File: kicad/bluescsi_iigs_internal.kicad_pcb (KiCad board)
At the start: 2 copper layers, 61.5 x 55.4 mm, 27 parts, among them J1 Conn_02x13_Odd_Even, J2 Conn_02x13_Odd_Even, J3 105162-0001, J4 Conn_01x02_Male, J5 Conn_01x02_Male, J6 DB25_Male, M1 Screw_Terminal_01x01, M2 Screw_Terminal_01x01, SW1 SW_SPDT, U1 YAAJ_BluePill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

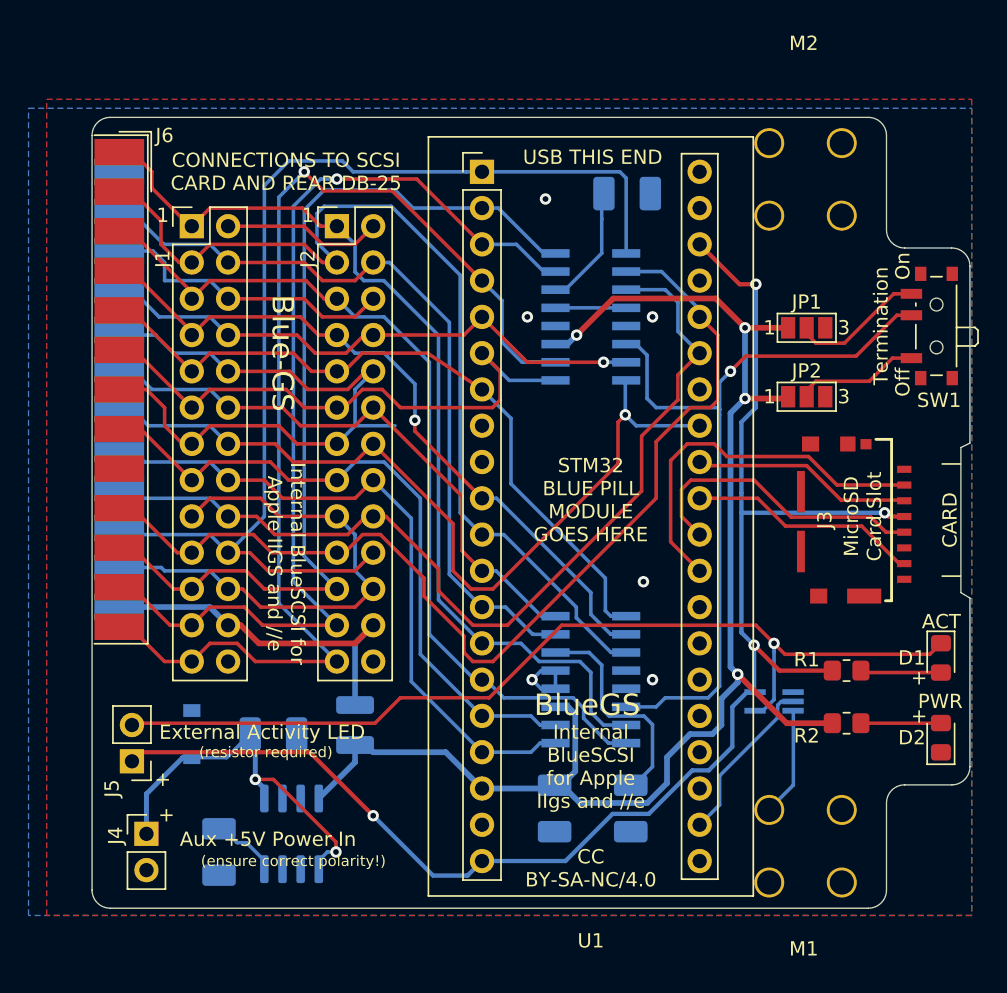
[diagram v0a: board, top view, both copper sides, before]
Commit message: Increase card indent, change C5 footprint
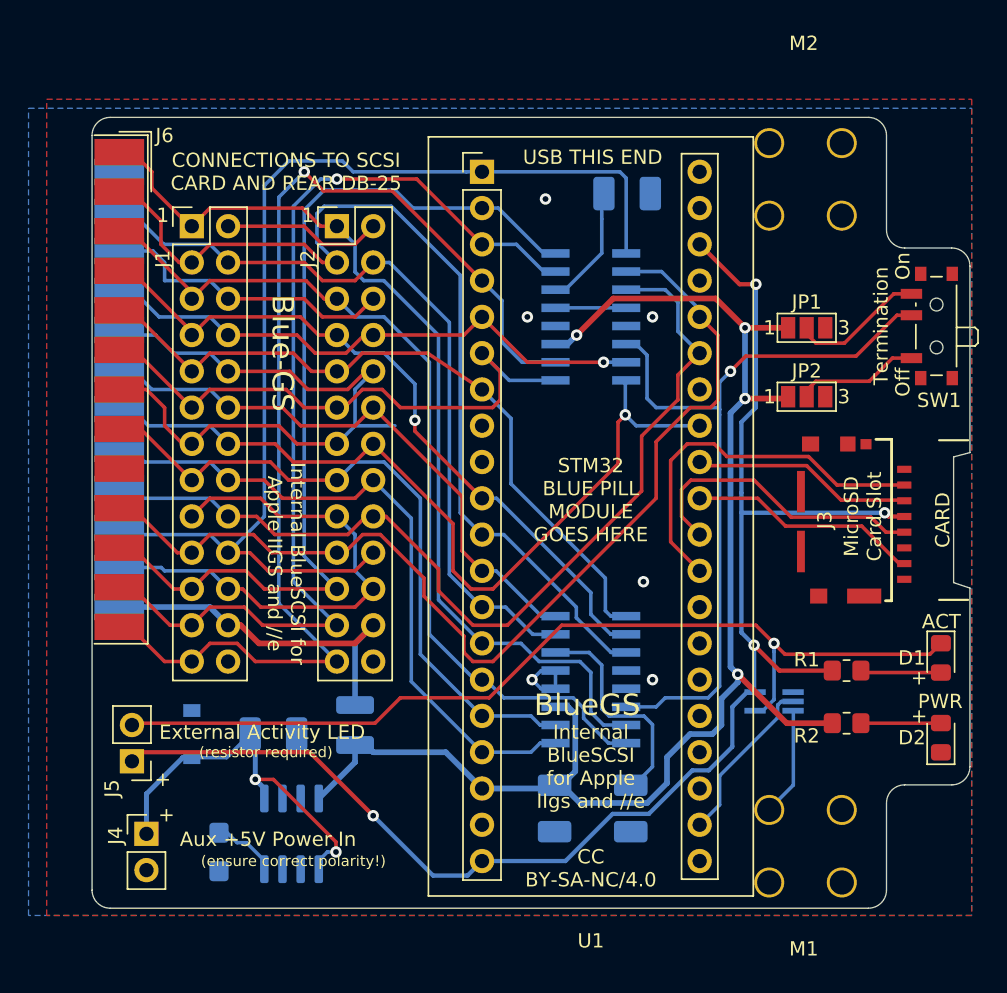
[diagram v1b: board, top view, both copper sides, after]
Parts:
- C1, C2: value 4.7uF, 6.3v -> 2.2uF, 6.3v
- C5: footprint Capacitor_Tantalum_SMD:CP_EIA-3528-21_Kemet-B_Pad1.50x2.35mm_HandSolder -> Capacitor_Tantalum_SMD:CP_EIA-3216-10_Kemet-I
- R1: value 110 -> 100
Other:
- outline, holes or cut-outs redrawn
- board text added: "CARD"
- board text removed: "| CARD |"

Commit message: Added compatibility for 74LVC1G125SE in place of NL17SZ07DFT2G
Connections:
- U5 pad 1: unconnected-(U5-Pad1) -> GND
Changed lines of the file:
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@@
   (net 51 "/SCSI_TERMPWR")
   (net 52 "Net-(D1-Pad2)")
-  (net 53 "unconnected-(U5-Pad1)")
   (footprint "my library:YAAJ_BluePill_2" (layer "F.Cu")
     (at 152.4 50.8)
@@
     (tags "capacitor tantalum")
     (property "DESCRIPTION" "2.2uF 6.3V CASE-B_3528 Tantalum Capacitor")
-    (property "LCSC part number" "C19276")
+    (property "LCSC part number" "C444753")
     (property "MANUFACTURER_NAME" "Kyocera AVX")
-    (property "MANUFACTURER_PART_NUMBER" "TAJB225K035RNJ")
+    (property "MANUFACTURER_PART_NUMBER" "TAJB225M020RNJ")
     (property "Sheetfile" "bluescsi_iigs_internal.kicad_sch")
     (property "Sheetname" "")
@@
     (tags "capacitor tantalum")
     (property "DESCRIPTION" "4.7uF 6.3V CASE-B_3528 Tantalum Capacitor")
-    (property "LCSC part number" "C7204")
-    (property "MANUFACTURER_NAME" "Kyocera AVX")
-    (property "MANUFACTURER_PART_NUMBER" "TAJB475K016RNJ")
+    (property "LCSC part number" "C918865")
+    (property "MANUFACTURER_NAME" "KEMET")
+    (property "MANUFACTURER_PART_NUMBER" "T494B475K016AT")
     (property "Sheetfile" "bluescsi_iigs_internal.kicad_sch")
     (property "Sheetname" "")
@@
     (tags "capacitor tantalum")
     (property "DESCRIPTION" "2.2uF 6.3V CASE-B_3528 Tantalum Capacitor")
-    (property "LCSC part number" "C19276")
+    (property "LCSC part number" "C444753")
     (property "MANUFACTURER_NAME" "Kyocera AVX")
-    (property "MANUFACTURER_PART_NUMBER" "TAJB225K035RNJ")
+    (property "MANUFACTURER_PART_NUMBER" "TAJB225M020RNJ")
     (property "Sheetfile" "bluescsi_iigs_internal.kicad_sch")
     (property "Sheetname" "")
@@
     (fp_line (start -0.675 0.6) (end -0.675 -1.1) (layer "B.Fab") (width 0.1))
     (pad "1" smd rect locked (at -1.33 0.65 180) (size 1.5 0.4) (layers "B.Cu" "B.Paste" "B.Mask")
-      (net 53 "unconnected-(U5-Pad1)") (pinfunction "Pin_1") (pintype "passive+no_connect"))
+      (net 13 "GND") (pinfunction "Pin_1") (pintype "passive"))
     (pad "2" smd rect locked (at -1.33 0 180) (size 1.5 0.4) (layers "B.Cu" "B.Paste" "B.Mask")
       (net 50 "/DISK_ACT") (pinfunction "Pin_2") (pintype "passive"))
@@
     (tags "capacitor tantalum")
     (property "DESCRIPTION" "1uF 6.3V CASE-B_3528 Tantalum Capacitor")
-    (property "LCSC part number" "C7192")
-    (property "MANUFACTURER_NAME" "Kyocera AVX")
-    (property "MANUFACTURER_PART_NUMBER" "TAJB105K035RNJ")
+    (property "LCSC part number" "C452761")
+    (property "MANUFACTURER_NAME" "KEMET")
+    (property "MANUFACTURER_PART_NUMBER" "T491B105K025AT")
     (property "Sheetfile" "bluescsi_iigs_internal.kicad_sch")
     (property "Sheetname" "")
@@
   )
   (gr_text "Internal BlueSCSI for\nApple IIGS and //e\n" (at 138.684 78.232 270) (layer "F.SilkS")
-    (effects (font (size 1 1) (thickness 0.15)))
+    (effects (font (size 1 1) (thickness 0.125)))
   )
   (gr_text "PWR" (at 186.055 87.884) (layer "F.SilkS")

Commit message: Push traces around, remove a hyphen
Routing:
- net +3V3: track 106.0 -> 105.2 mm, vias 4 -> 3
- net /SCSI_RST: track 50.1 -> 49.5 mm
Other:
- board text removed: "Blue-GS"

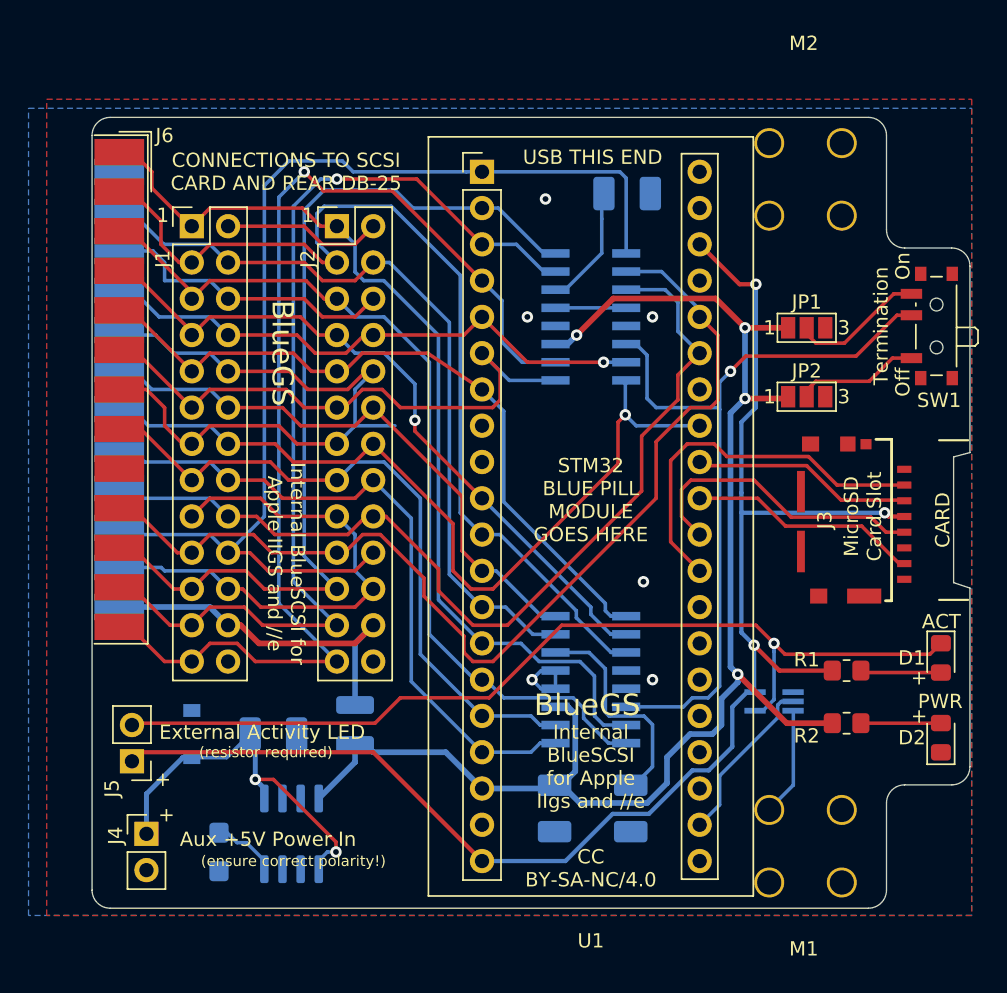
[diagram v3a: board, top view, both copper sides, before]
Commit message: Make name more consistent, move sinkscreens around to make things look better
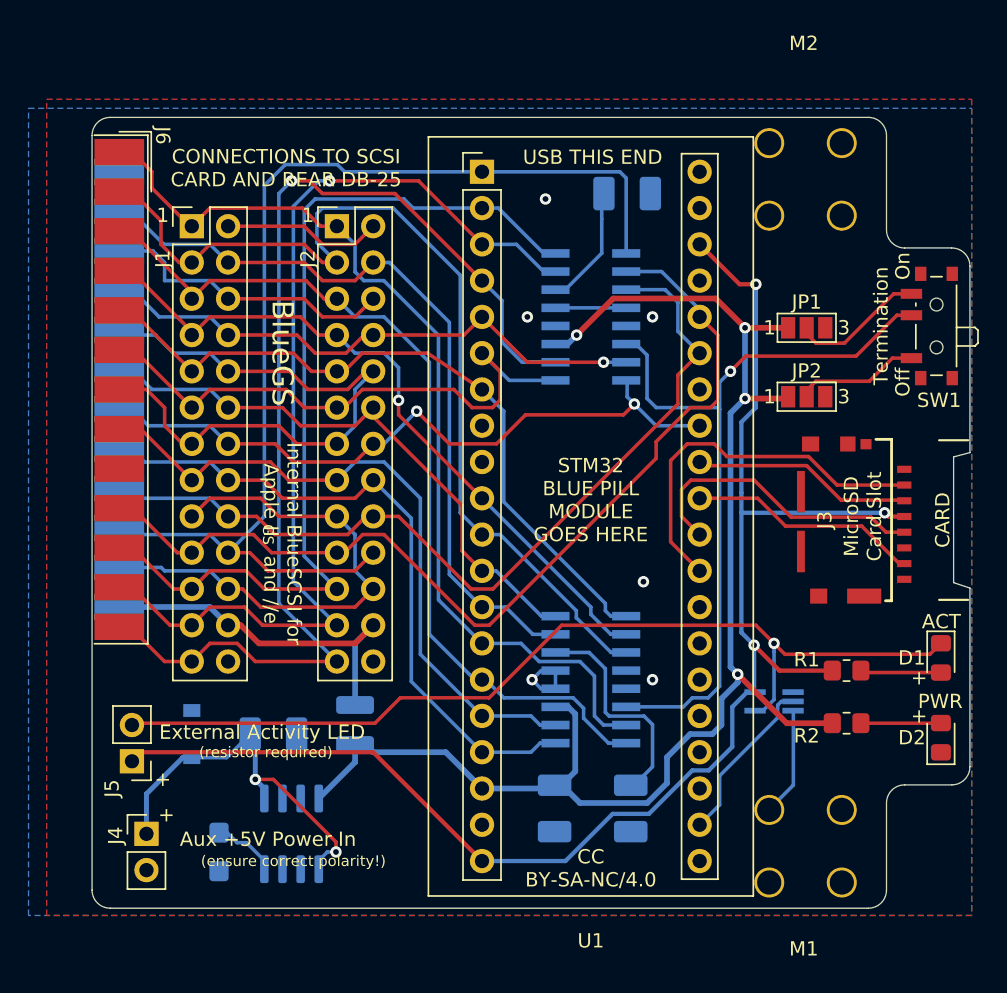
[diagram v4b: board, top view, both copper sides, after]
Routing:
- net /SCSI_DBP: track 58.3 -> 48.1 mm, vias 1 -> 2
- net /SCSI_DB3: track 72.9 -> 67.7 mm
- net /SCSI_DB2: track 65.9 -> 60.8 mm
- net GND: track 134.2 -> 131.4 mm
- net /SCSI_DB5: track 65.0 -> 64.5 mm
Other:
- board text added: "GS"
- board text added: "Internal BlueSCSI for Apple II and //e"
- board text added: "v1.4 (12/2022)"
- board text removed: "Internal BlueSCSI for Apple IIGS and //e"
- board text removed: "Internal BlueSCSI for Apple IIgs and //e"
- board text removed: "v1.4 (11/2022)"

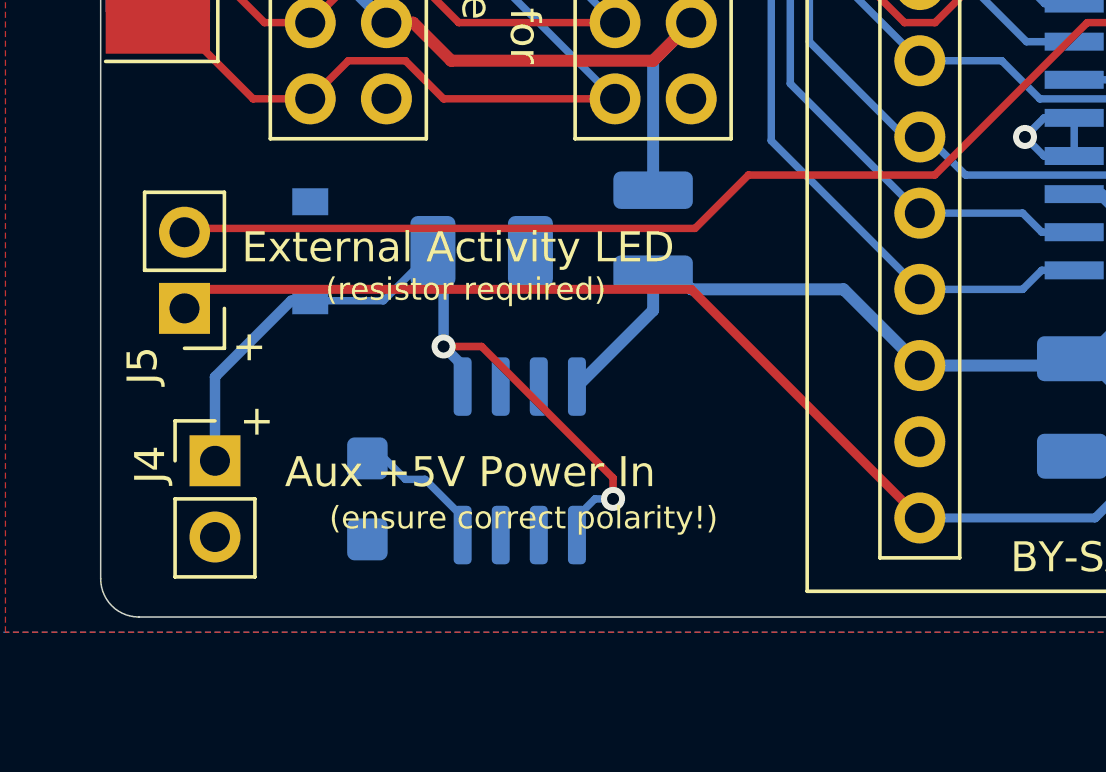
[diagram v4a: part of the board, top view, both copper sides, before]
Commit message: Move power controller to front for better wire clearance in tight cases
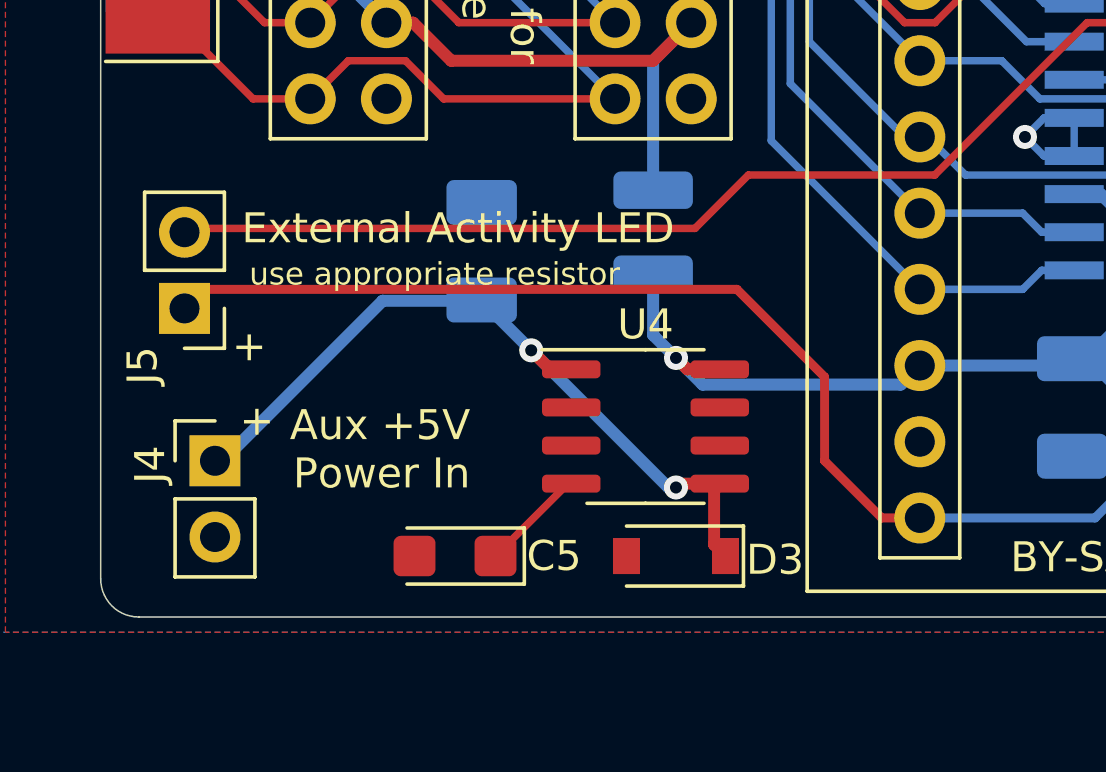
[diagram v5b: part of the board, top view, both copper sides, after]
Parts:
- C5, D3, U4: moved to F.Cu
- moved D3 15.9 mm to (144.3, 100.3), turned to 180 degrees
- moved U4 4.34 mm to (143.3, 96.0), turned to 0 degrees
- moved C5 3.49 mm to (136.9, 100.3), turned to 180 degrees
- turned C4 to 90 degrees
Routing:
- net +3V3: track 105.2 -> 106.8 mm
- net +5V: track 101.7 -> 100.2 mm, vias 4 -> 5
- net Net-(C5-Pad1): track 4.70 -> 3.52 mm
- net /+5V_AUX: track 26.9 -> 25.9 mm
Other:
- board text added: "check the polarity!"
- board text added: "use appropriate resistor"
- board text removed: "(ensure correct polarity!)"
- board text removed: "(resistor required)"

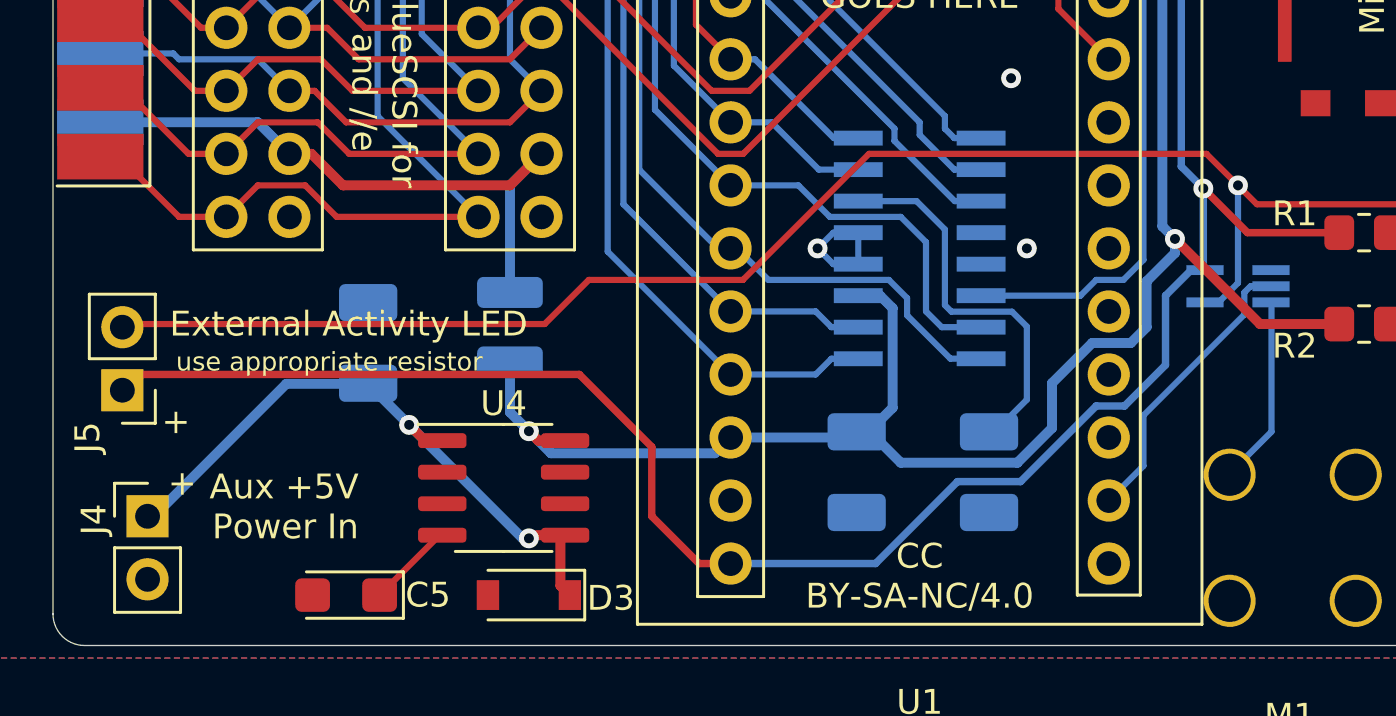
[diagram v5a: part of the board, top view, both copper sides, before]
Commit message: Move Termpower decoupling cap closer to the connector (as per specs)
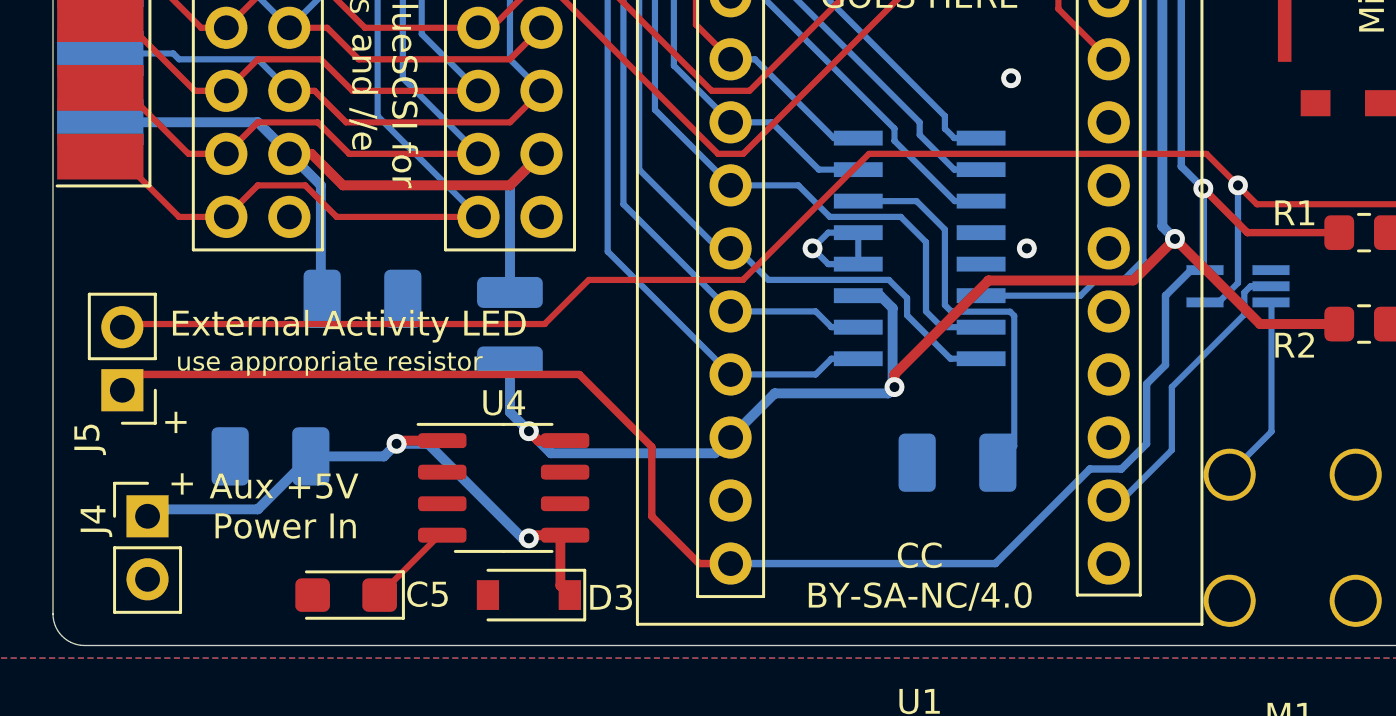
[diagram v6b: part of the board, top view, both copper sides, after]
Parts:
- moved C3 21.1 mm to (137.6, 88.4), turned to 0 degrees
- moved C4 6.03 mm to (133.9, 94.7), turned to 180 degrees
- moved C2 1.33 mm to (161.5, 95.0), turned to 180 degrees
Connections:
- C3 pad 1: +5V -> /SCSI_TERMPWR
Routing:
- net +5V: track 100.2 -> 94.3 mm, vias 5 -> 6
- net /SCSI_TERMPWR: track 25.5 -> 31.2 mm
- net /+5V_AUX: track 25.9 -> 24.2 mm
- net +3V3: track 106.8 -> 108.2 mm
- net Net-(C2-Pad1): track 15.1 -> 16.2 mm
